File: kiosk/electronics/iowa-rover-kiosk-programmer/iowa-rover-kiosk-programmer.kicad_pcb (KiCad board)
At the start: 2 copper layers, 151.1 x 31.8 mm, 21 parts, among them J1 Conn_02x06_Odd_Even, SW1 SW_Push, SW2 SW_Push, SW3 SW_Push, SW4 SW_Push, SW5 SW_Push, U1 ID12-LA

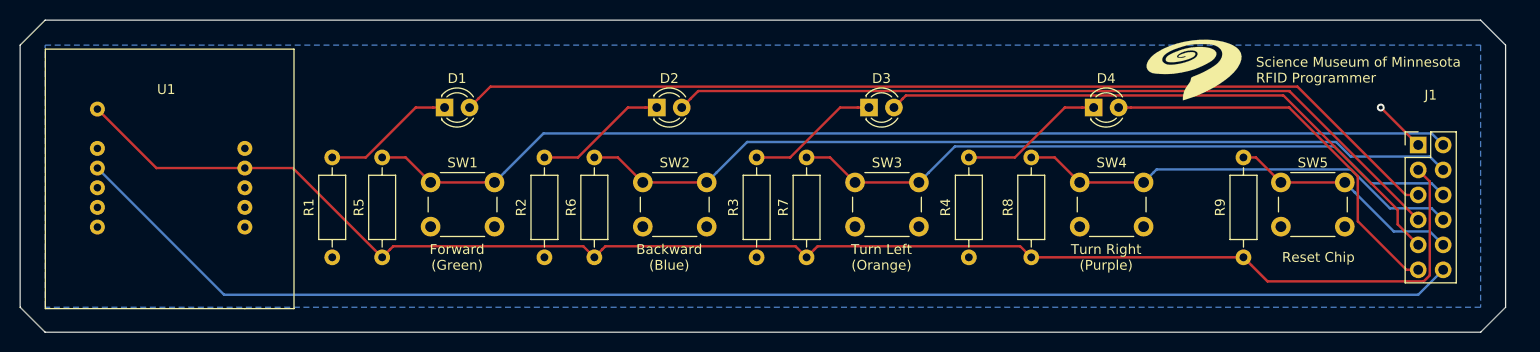
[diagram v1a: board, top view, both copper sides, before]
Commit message: initial pass at board drawings
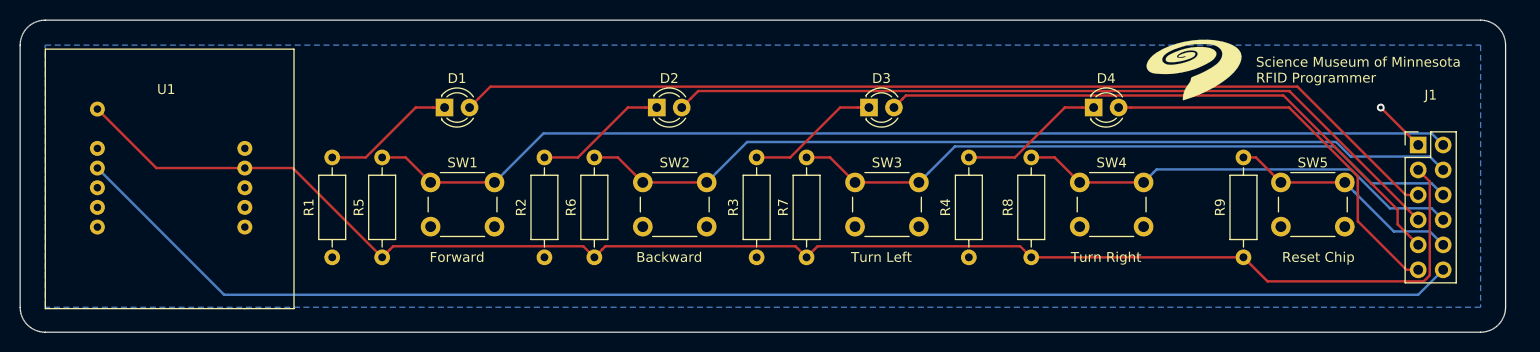
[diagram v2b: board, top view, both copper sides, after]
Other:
- board text added: "Backward"
- board text added: "Forward"
- board text added: "Turn Left"
- board text added: "Turn Right"
- board text removed: "Backward (Blue)"
- board text removed: "Forward (Green)"
- board text removed: "Turn Left (Orange)"
- board text removed: "Turn Right (Purple)"
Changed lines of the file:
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@@
   (gr_line (start 67.31 67.31) (end 67.31 93.98)
     (stroke (width 0.1) (type solid)) (layer "Edge.Cuts"))
-  (gr_line (start 67.31 93.98) (end 69.85 96.52)
-    (stroke (width 0.1) (type solid)) (layer "Edge.Cuts"))
+  (gr_arc (start 218.44 93.98) (mid 217.696051 95.776051) (end 215.9 96.52)
+    (stroke (width 0.1) (type default)) (layer "Edge.Cuts"))
   (gr_line (start 218.44 93.98) (end 218.44 67.31)
     (stroke (width 0.1) (type solid)) (layer "Edge.Cuts"))
   (gr_line (start 215.9 64.77) (end 69.85 64.77)
     (stroke (width 0.1) (type solid)) (layer "Edge.Cuts"))
-  (gr_line (start 215.9 96.52) (end 218.44 93.98)
-    (stroke (width 0.1) (type solid)) (layer "Edge.Cuts"))
-  (gr_line (start 69.85 64.77) (end 67.31 67.31)
-    (stroke (width 0.1) (type solid)) (layer "Edge.Cuts"))
-  (gr_line (start 218.44 67.31) (end 215.9 64.77)
-    (stroke (width 0.1) (type solid)) (layer "Edge.Cuts"))
+  (gr_arc (start 67.31 67.31) (mid 68.053949 65.513949) (end 69.85 64.77)
+    (stroke (width 0.1) (type default)) (layer "Edge.Cuts"))
+  (gr_arc (start 215.9 64.77) (mid 217.696051 65.513949) (end 218.44 67.31)
+    (stroke (width 0.1) (type default)) (layer "Edge.Cuts"))
+  (gr_arc (start 69.85 96.52) (mid 68.053949 95.776051) (end 67.31 93.98)
+    (stroke (width 0.1) (type default)) (layer "Edge.Cuts"))
   (gr_line (start 69.85 96.52) (end 215.9 96.52)
     (stroke (width 0.1) (type solid)) (layer "Edge.Cuts"))
@@
     (effects (font (size 1 1) (thickness 0.15)))
   )
-  (gr_text "Backward\n(Blue)" (at 133.35 88.9) (layer "F.SilkS")
+  (gr_text "Backward" (at 133.35 88.9) (layer "F.SilkS")
     (effects (font (size 1 1) (thickness 0.15)))
   )
-  (gr_text "Forward\n(Green)" (at 111.76 88.9) (layer "F.SilkS")
+  (gr_text "Forward" (at 111.76 88.9) (layer "F.SilkS")
     (effects (font (size 1 1) (thickness 0.15)))
   )
-  (gr_text "Turn Right\n(Purple)" (at 177.8 88.9) (layer "F.SilkS")
+  (gr_text "Turn Right" (at 177.8 88.9) (layer "F.SilkS")
     (effects (font (size 1 1) (thickness 0.15)))
   )
-  (gr_text "Turn Left\n(Orange)" (at 154.94 88.9) (layer "F.SilkS")
+  (gr_text "Turn Left" (at 154.94 88.9) (layer "F.SilkS")
     (effects (font (size 1 1) (thickness 0.15)))
   )
